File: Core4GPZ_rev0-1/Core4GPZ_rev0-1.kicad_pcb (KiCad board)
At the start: 2 copper layers, 91.4 x 105.4 mm, 37 parts, among them IC1 MAX9926UAEE_V+, M3 MountingHole_3.2mm_M3_DIN965_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, Q1 FGP3440G2-F085, Q2 FGP3440G2-F085, U2 core4, U3 MPX4250

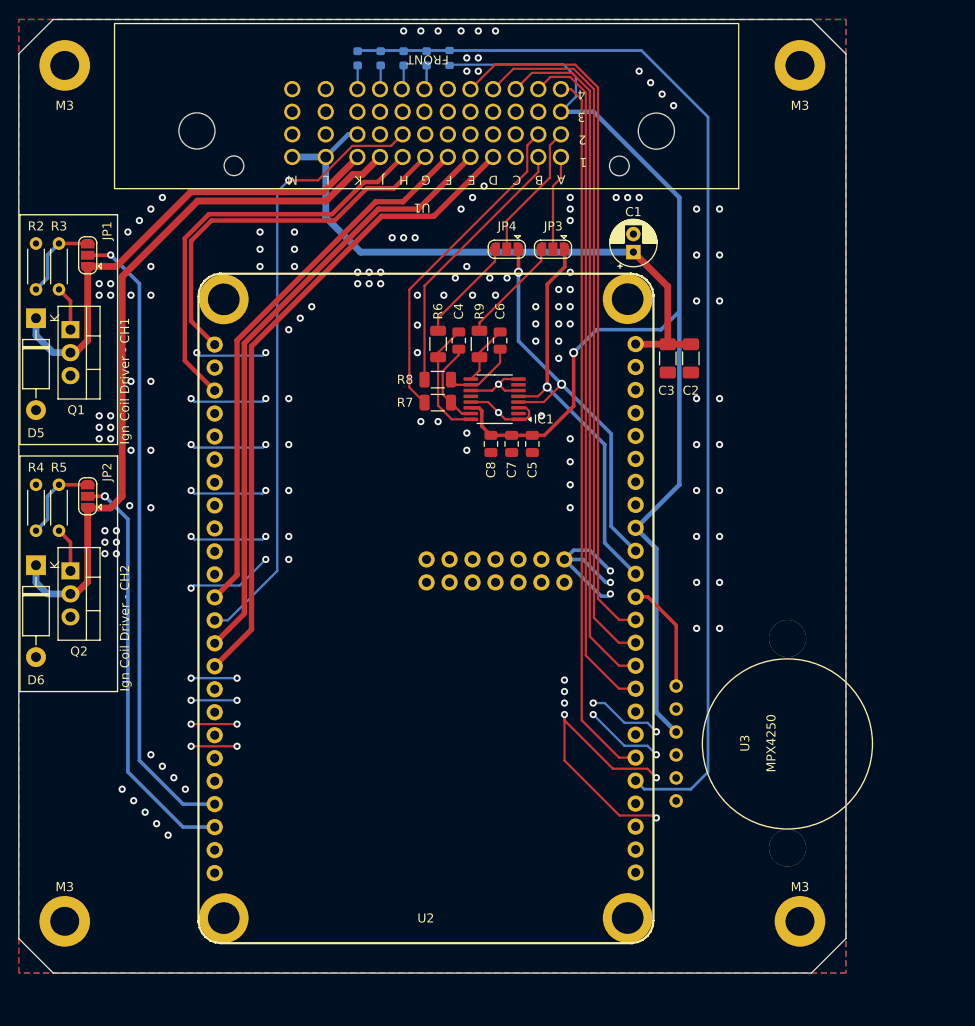
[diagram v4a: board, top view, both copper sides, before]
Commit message: Moved VR Conditionner.
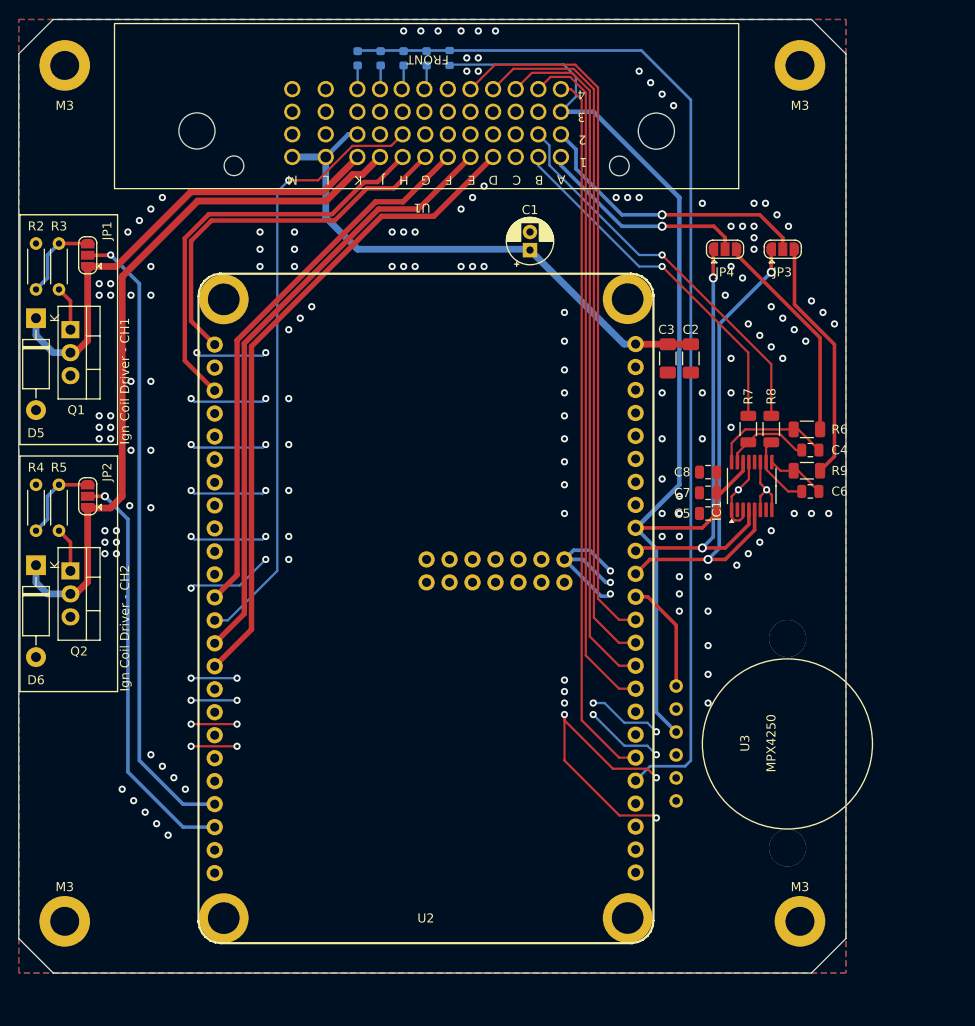
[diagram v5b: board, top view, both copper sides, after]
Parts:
- moved R6 41.8 mm to (146.2, 72.0), turned to 180 degrees
- moved C4 40.7 mm to (146.6, 74.3), turned to 180 degrees
- moved R9 38.8 mm to (146.2, 76.6), turned to 180 degrees
- moved C6 38.1 mm to (146.6, 78.8), turned to 0 degrees
- moved R8 37.3 mm to (142.2, 71.9), turned to -90 degrees
- moved R7 34.5 mm to (139.7, 71.9), turned to -90 degrees
- moved IC1 30.0 mm to (140.1, 78.2), turned to 90 degrees
- moved JP3 25.4 mm to (143.5, 52.1), turned to 0 degrees
- moved C8 24.2 mm to (135.3, 76.7), turned to 180 degrees
- moved JP4 24.1 mm to (137.1, 52.1), turned to 0 degrees
- moved C7 22.4 mm to (135.3, 79.0), turned to 180 degrees
- moved C5 20.9 mm to (135.3, 81.3), turned to 180 degrees
- moved C1 11.4 mm to (115.6, 52.2)
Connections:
- U1 pad 1: CAM_SNSR -> CRANK_SNSR
- U1 pad 11: CRANK_SNSR -> CAM_SNSR
- U1 pad 12: CRANK_SNSR_VR- -> CAM_SNSR_VR-
- U1 pad 2: CAM_SNSR_VR- -> CRANK_SNSR_VR-
- U2 pad : (no net) -> BIKE_GROUND
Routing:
- net CAM_SNSR: track 10.9 -> 31.8 mm, vias 0 -> 1
- net SNSR_+5V: track 133.5 -> 118.1 mm, vias 1 -> 0
- net Net-(JP3-B): track 11.8 -> 27.0 mm
- net CAM_SNSR_VR-: track 29.9 -> 43.3 mm, vias 0 -> 1
- net Net-(JP4-B): track 11.6 -> 23.7 mm
- net CAM_SIGNAL: track 44.4 -> 54.6 mm, vias 1 -> 2
- net CRANK_SNSR: track 15.2 -> 24.0 mm, vias 0 -> 1
- net BIKE_+12V_SWITCHED_IN: track 68.4 -> 61.1 mm
- net CRANK_SIGNAL: track 44.3 -> 48.9 mm
- net SAFE_SIGNAL: track 123.4 -> 119.2 mm
- net CRANK_SNSR_VR-: track 36.4 -> 40.1 mm, vias 0 -> 1
- net BIKE_GROUND: vias 168 -> 177

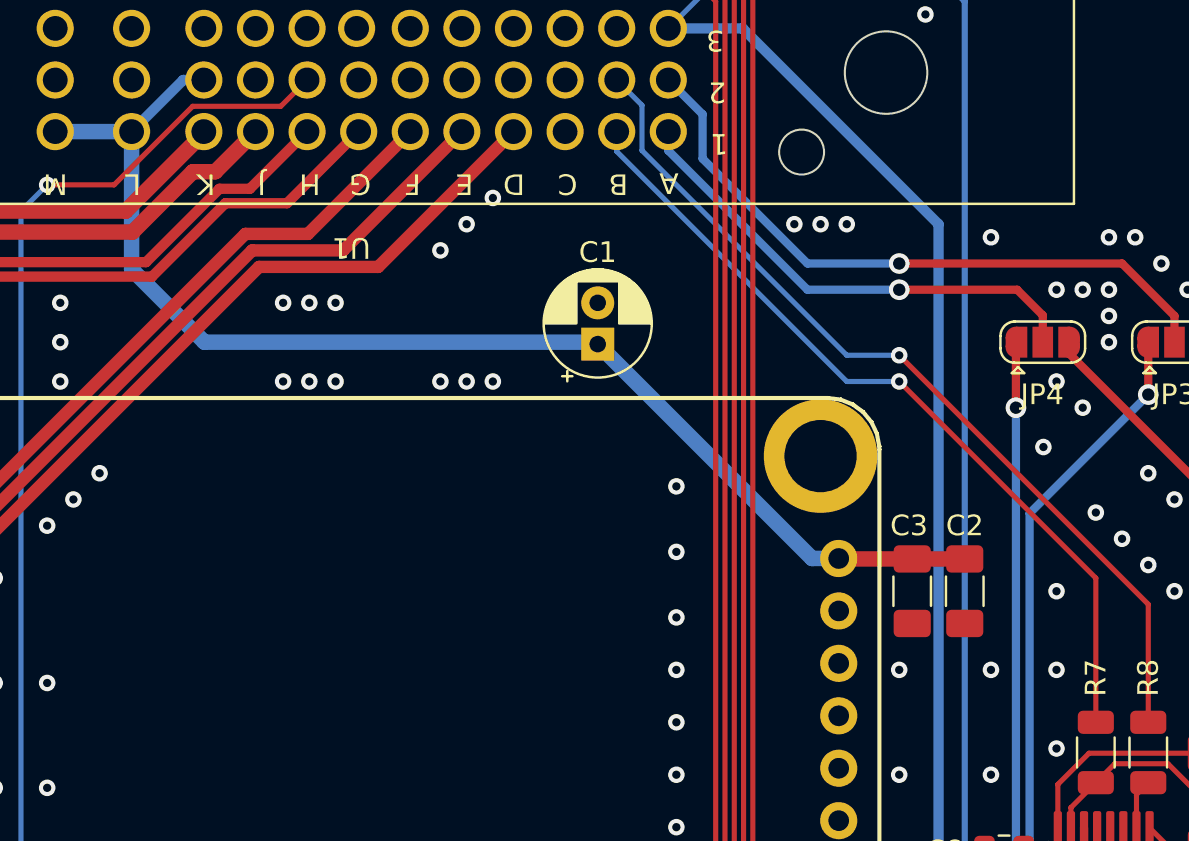
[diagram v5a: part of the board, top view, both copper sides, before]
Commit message: Moved +12V decoupling capacitors
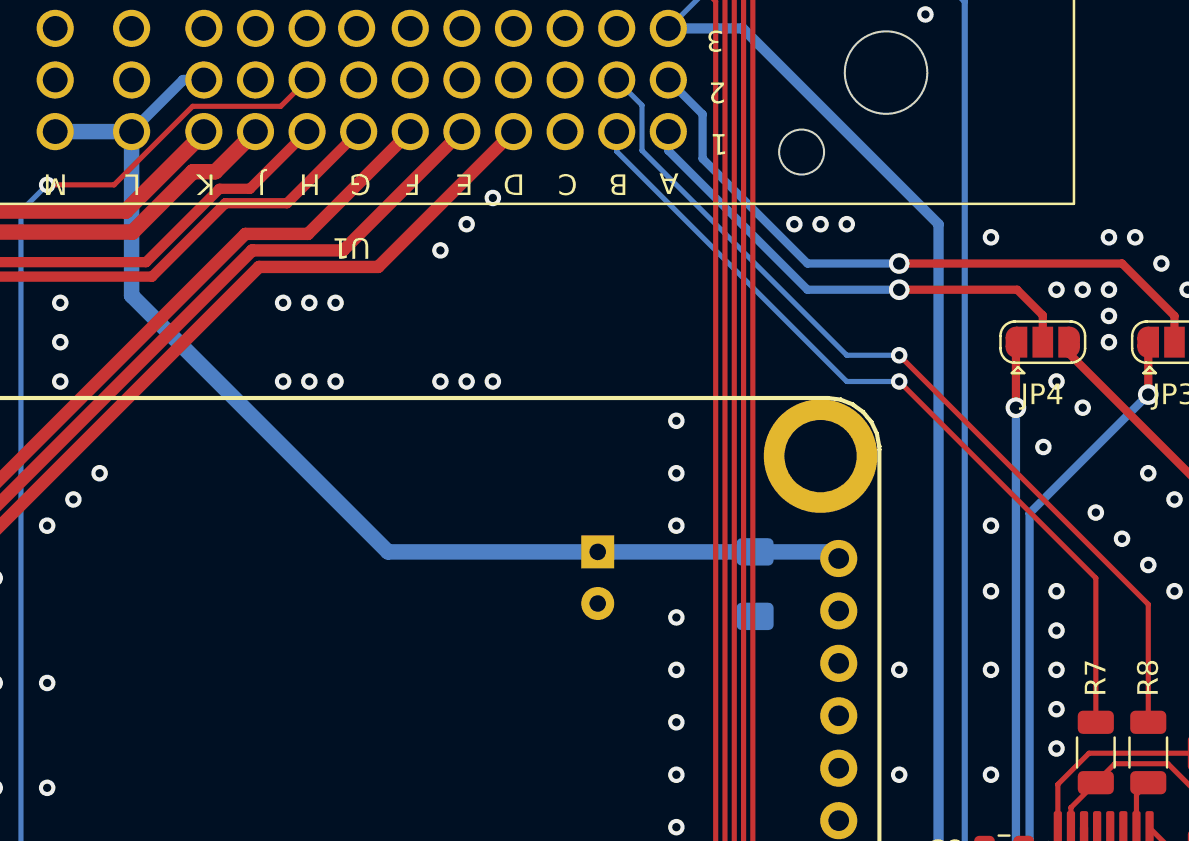
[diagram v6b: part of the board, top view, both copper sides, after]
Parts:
- removed C3: 1nF, Capacitor_SMD:C_1206_3216Metric_Pad1.33x1.80mm_HandSolder
- C1: footprint Capacitor_THT:CP_Radial_D5.0mm_P2.00mm -> Capacitor_THT:CP_Radial_D5.0mm_P2.50mm; moved to B.Cu
- C2: moved to B.Cu
- moved C2 10.2 mm to (123.2, 63.8)
- moved C1 10.1 mm to (115.6, 62.2), turned to -90 degrees
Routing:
- net BIKE_+12V_SWITCHED_IN: track 61.1 -> 55.8 mm
- net BIKE_GROUND: vias 177 -> 182

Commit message: Changed MAP sensors for MPXHZ6250AC6T1
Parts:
- added C3: 1uF, Capacitor_SMD:C_0805_2012Metric_Pad1.18x1.45mm_HandSolder, B.Cu at (134.4, 39.2)
- added C9: 100nF, Capacitor_SMD:C_0805_2012Metric_Pad1.18x1.45mm_HandSolder, B.Cu at (134.4, 36.2)
- U3: value MPX4250 -> MPXHZ6250AC6T1; footprint Misc:MPX4250 -> IC_Automotive:MPXHZ6250AC6T1
- moved U3 7.34 mm to (139.1, 100.3)
- moved C5 0.71 mm to (134.9, 80.6)
- moved C7 0.71 mm to (134.9, 78.4)
- moved C8 0.71 mm to (134.9, 76.1)
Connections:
- U2 pad : BIKE_GROUND -> (no net)
- U3 pad 1: Net-(U2B-MAP_IN) -> (no net)
- U3 pad 2: BIKE_GROUND -> SNSR_+5V
- U3 pad 3: SNSR_+5V -> BIKE_GROUND
- U3 pad 4: (no net) -> Net-(U2B-MAP_IN)
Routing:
- net Net-(U2B-MAP_IN): track 12.9 -> 12.4 mm
- net SNSR_+5V: vias 0 -> 1
- net BIKE_GROUND: vias 182 -> 189

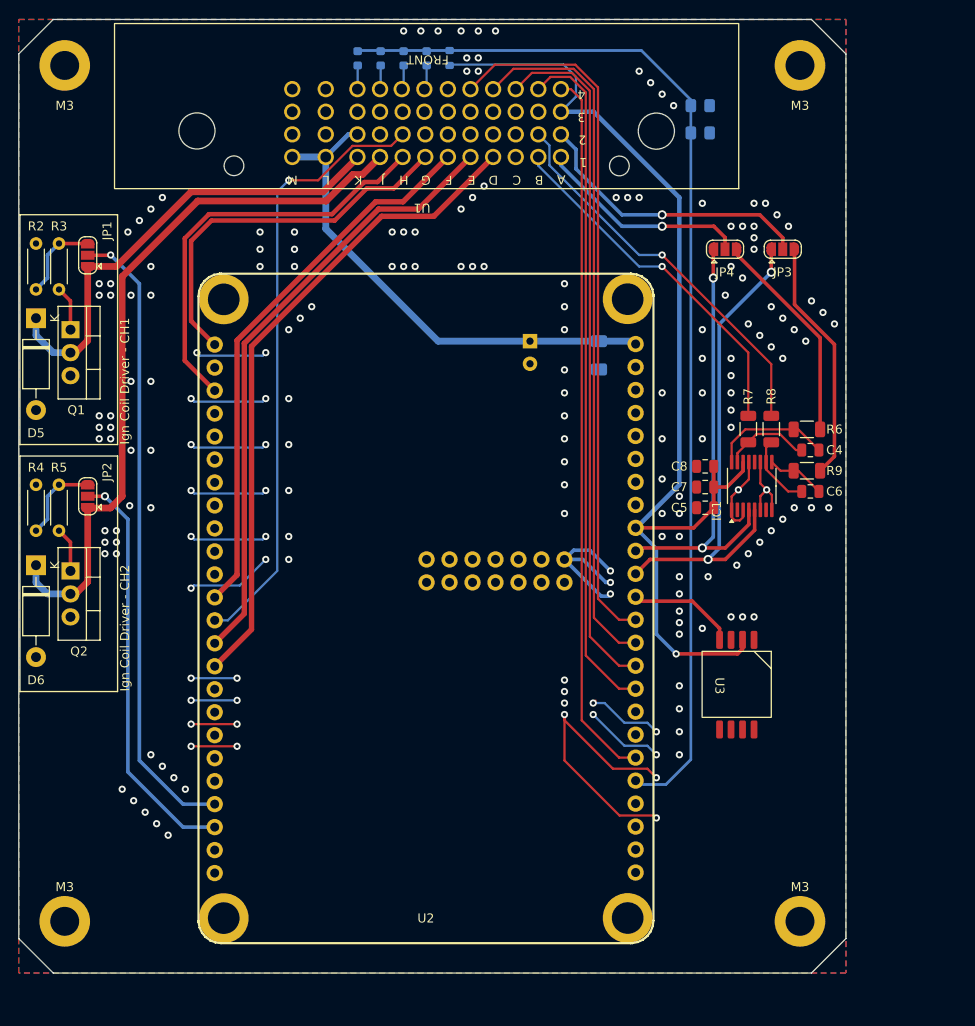
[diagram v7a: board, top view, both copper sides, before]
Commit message: Modified GND Plane. Reworked routing
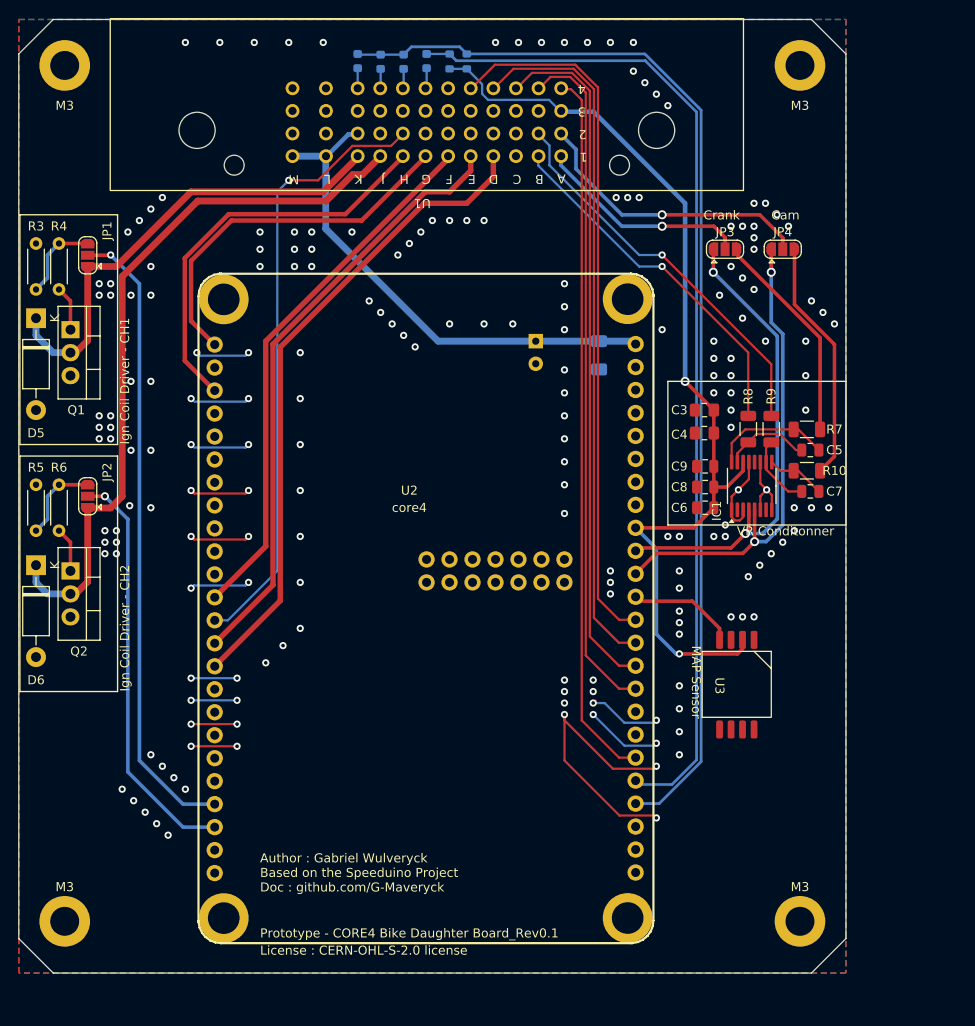
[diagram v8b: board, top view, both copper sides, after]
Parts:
- added R2: 100k, Resistor_SMD:R_0603_1608Metric, B.Cu at (106.7, 31.3)
- C3: renamed from C9; moved to F.Cu
- C4: renamed from C3; moved to F.Cu
- moved C3 33.7 mm to (134.9, 69.8), turned to 180 degrees
- moved C4 33.2 mm to (134.9, 72.4), turned to 180 degrees
- moved D4 5.09 mm to (104.1, 31.3)
- moved D3 2.57 mm to (101.6, 31.3)
- moved D2 2.57 mm to (99.1, 31.3)
- moved U1 2.41 mm to (104.0, 29.1)
- moved R1 1.94 mm to (108.6, 31.3)
- moved C1 0.64 mm to (116.2, 62.2)
- moved D1 0.30 mm to (96.5, 31.3)
- renumbered C4 to C5, C5 to C6, C6 to C7, C7 to C8, C8 to C9, D3 to D2, D4 to D3, D2 to D4, JP4 to JP3, JP3 to JP4, R9 to R10, R2 to R3, R3 to R4, R4 to R5, R5 to R6, R6 to R7, R7 to R8, R8 to R9
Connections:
- D4 pad 2: SAFE_SIGNAL -> NEUTRAL_SIGNAL
- U1 pad 36: SPR2_SWITCH -> unconnected-(U1B-4F-Pad36)
- U1 pad 37: SPR1_SWITCH -> Neutral_SWITCH
- U1 pad 38: Clutch_SWITCH -> SPR1_SWITCH
- U1 pad 39: Neutral_SWITCH -> Clutch_SWITCH
- U2 pad 44: SAFE_SIGNAL -> NEUTRAL_SIGNAL
- U2 pad 45: NEUTRAL_SIGNAL -> SAFE_SIGNAL
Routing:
- net NEUTRAL_SIGNAL: track 0.00 -> 112.2 mm
- net BIKE_GROUND: track 157.7 -> 124.9 mm, vias 189 -> 194
- net SNSR_+5V: track 118.1 -> 106.7 mm, vias 1 -> 2
- net CRANK_SIGNAL: track 48.9 -> 52.6 mm
- net SAFE_SIGNAL: track 119.5 -> 122.4 mm
- net /IDLE_1: track 61.1 -> 59.6 mm
- net CAM_SIGNAL: track 54.6 -> 53.0 mm
- net /FAN_CTL: track 73.2 -> 71.9 mm
- net /INJ2_TRIG: track 46.7 -> 45.4 mm
- net /INJ1_TRIG: track 42.3 -> 41.0 mm
- net /FUEL_PUMP: track 68.1 -> 67.1 mm
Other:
- outline, holes or cut-outs redrawn
- board text added: "Author : Gabriel Wulveryck Based on the Speeduino Project Doc : github.com/G-Maveryck"
- board text added: "Cam"
- board text added: "Crank"
- board text added: "D"
- board text added: "License : CERN-OHL-S-2.0 license"
- board text added: "MAP Sensor"
- board text added: "Prototype - CORE4 Bike Daughter Board_Rev0.1"
- board text added: "VR Conditonner"
